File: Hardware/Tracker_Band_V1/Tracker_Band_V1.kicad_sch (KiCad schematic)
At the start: 79 parts, among them J1 USB_C_USB20, Q1 SSM6L56FE, SW1 EVP-AVAA1A, SW2 EVP-AVAA1A, U1 ESP32-C3-MINI-1-N4, U2 BNO085, U3 RT8010, U4 MCP73832-2-AC, U5 LM66200, U6 IN-PI15TAT5R5G5B, U7 IN-PI15TAT5R5G5B, U8 IN-PI15TAT5R5G5B, U9 IN-PI15TAT5R5G5B, X1 32.768kHz

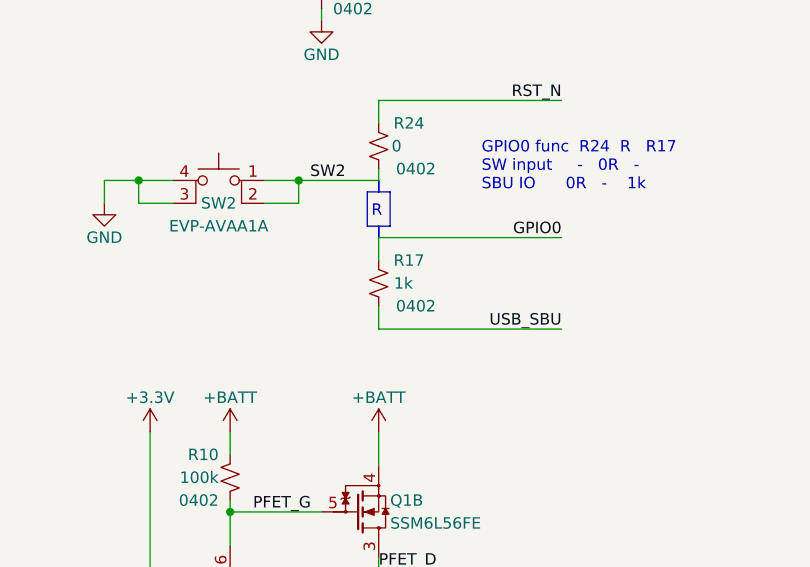
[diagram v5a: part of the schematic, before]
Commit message: Component ordering information finalized
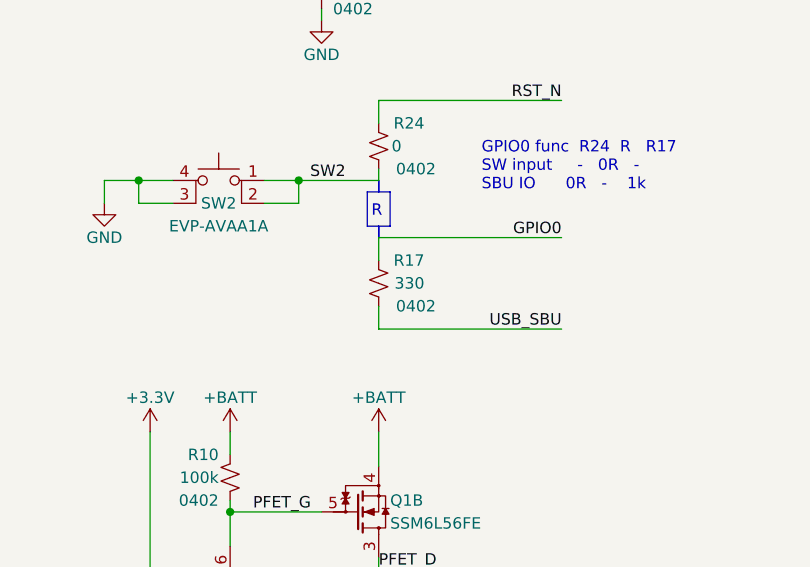
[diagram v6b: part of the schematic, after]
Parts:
- LG1, TP1, TP10, TP11, TP12, TP13, TP14, TP15, TP16, TP17, TP18, TP19, TP2, TP20, TP21, TP3, TP4, TP5, TP6, TP7, TP8, TP9: now left out of the parts list
- R17: value 1k -> 330
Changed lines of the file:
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@@
   )
   (symbol (lib_id "Connector:TestPoint") (at 355.6 81.28 270) (unit 1)
-    (in_bom yes) (on_board yes) (dnp no)
+    (in_bom no) (on_board yes) (dnp no)
     (property "Reference" "TP19" (at 365.76 81.28 90)
       (effects (font (size 1.27 1.27)) (justify left))
@@
   )
   (symbol (lib_id "Connector:TestPoint") (at 355.6 68.58 270) (unit 1)
-    (in_bom yes) (on_board yes) (dnp no)
+    (in_bom no) (on_board yes) (dnp no)
     (property "Reference" "TP14" (at 365.76 68.58 90)
       (effects (font (size 1.27 1.27)) (justify left))
@@
   )
   (symbol (lib_id "Connector:TestPoint") (at 355.6 66.04 270) (unit 1)
-    (in_bom yes) (on_board yes) (dnp no)
+    (in_bom no) (on_board yes) (dnp no)
     (property "Reference" "TP13" (at 365.76 66.04 90)
       (effects (font (size 1.27 1.27)) (justify left))
@@
   )
   (symbol (lib_id "Connector:TestPoint") (at 147.32 260.35 270) (unit 1)
-    (in_bom yes) (on_board yes) (dnp no)
+    (in_bom no) (on_board yes) (dnp no)
     (property "Reference" "TP4" (at 160.02 260.35 90)
       (effects (font (size 1.27 1.27)) (justify left))
@@
   )
   (symbol (lib_id "Connector:TestPoint") (at 355.6 55.88 270) (unit 1)
-    (in_bom yes) (on_board yes) (dnp no)
+    (in_bom no) (on_board yes) (dnp no)
     (property "Reference" "TP9" (at 365.76 55.88 90)
       (effects (font (size 1.27 1.27)) (justify left))
@@
   )
   (symbol (lib_id "Connector:TestPoint") (at 147.32 255.27 270) (unit 1)
-    (in_bom yes) (on_board yes) (dnp no)
+    (in_bom no) (on_board yes) (dnp no)
     (property "Reference" "TP2" (at 160.02 255.27 90)
       (effects (font (size 1.27 1.27)) (justify left))
@@
   )
   (symbol (lib_id "Connector:TestPoint") (at 355.6 53.34 270) (unit 1)
-    (in_bom yes) (on_board yes) (dnp no)
+    (in_bom no) (on_board yes) (dnp no)
     (property "Reference" "TP8" (at 365.76 53.34 90)
       (effects (font (size 1.27 1.27)) (justify left))
@@
   )
   (symbol (lib_id "Connector:TestPoint") (at 355.6 105.41 270) (unit 1)
-    (in_bom yes) (on_board yes) (dnp no)
+    (in_bom no) (on_board yes) (dnp no)
     (property "Reference" "TP5" (at 368.3 105.41 90)
       (effects (font (size 1.27 1.27)) (justify left))
@@
   )
   (symbol (lib_id "Connector:TestPoint") (at 355.6 78.74 270) (unit 1)
-    (in_bom yes) (on_board yes) (dnp no)
+    (in_bom no) (on_board yes) (dnp no)
     (property "Reference" "TP18" (at 365.76 78.74 90)
       (effects (font (size 1.27 1.27)) (justify left))
@@
   )
   (symbol (lib_id "Connector:TestPoint") (at 355.6 107.95 270) (unit 1)
-    (in_bom yes) (on_board yes) (dnp no)
+    (in_bom no) (on_board yes) (dnp no)
     (property "Reference" "TP6" (at 368.3 107.95 90)
       (effects (font (size 1.27 1.27)) (justify left))
@@
   )
   (symbol (lib_id "Connector:TestPoint") (at 355.6 86.36 270) (unit 1)
-    (in_bom yes) (on_board yes) (dnp no)
+    (in_bom no) (on_board yes) (dnp no)
     (property "Reference" "TP21" (at 365.76 86.36 90)
       (effects (font (size 1.27 1.27)) (justify left))
@@
   )
   (symbol (lib_id "Connector:TestPoint") (at 355.6 76.2 270) (unit 1)
-    (in_bom yes) (on_board yes) (dnp no)
+    (in_bom no) (on_board yes) (dnp no)
     (property "Reference" "TP17" (at 365.76 76.2 90)
       (effects (font (size 1.27 1.27)) (justify left))
@@
   )
   (symbol (lib_id "Connector:TestPoint") (at 355.6 71.12 270) (unit 1)
-    (in_bom yes) (on_board yes) (dnp no)
+    (in_bom no) (on_board yes) (dnp no)
     (property "Reference" "TP15" (at 365.76 71.12 90)
       (effects (font (size 1.27 1.27)) (justify left))
@@
   )
   (symbol (lib_id "Connector:TestPoint") (at 355.6 60.96 270) (unit 1)
-    (in_bom yes) (on_board yes) (dnp no)
+    (in_bom no) (on_board yes) (dnp no)
     (property "Reference" "TP11" (at 365.76 60.96 90)
       (effects (font (size 1.27 1.27)) (justify left))
@@
   )
   (symbol (lib_id "Connector:TestPoint") (at 147.32 252.73 270) (unit 1)
-    (in_bom yes) (on_board yes) (dnp no)
+    (in_bom no) (on_board yes) (dnp no)
     (property "Reference" "TP1" (at 160.02 252.73 90)
       (effects (font (size 1.27 1.27)) (justify left))
@@
   )
   (symbol (lib_id "Connector:TestPoint") (at 355.6 58.42 270) (unit 1)
-    (in_bom yes) (on_board yes) (dnp no)
+    (in_bom no) (on_board yes) (dnp no)
     (property "Reference" "TP10" (at 365.76 58.42 90)
       (effects (font (size 1.27 1.27)) (justify left))
@@
   )
   (symbol (lib_id "Connector:TestPoint") (at 355.6 73.66 270) (unit 1)
-    (in_bom yes) (on_board yes) (dnp no)
+    (in_bom no) (on_board yes) (dnp no)
     (property "Reference" "TP16" (at 365.76 73.66 90)
       (effects (font (size 1.27 1.27)) (justify left))
@@
   )
   (symbol (lib_id "Connector:TestPoint") (at 355.6 50.8 270) (unit 1)
-    (in_bom yes) (on_board yes) (dnp no)
+    (in_bom no) (on_board yes) (dnp no)
     (property "Reference" "TP7" (at 365.76 50.8 90)
       (effects (font (size 1.27 1.27)) (justify left))
@@
   )
   (symbol (lib_id "Connector:TestPoint") (at 147.32 257.81 270) (unit 1)
-    (in_bom yes) (on_board yes) (dnp no)
+    (in_bom no) (on_board yes) (dnp no)
     (property "Reference" "TP3" (at 160.02 257.81 90)
       (effects (font (size 1.27 1.27)) (justify left))
@@
   )
   (symbol (lib_id "00_tracker_sym:AB_LOGO") (at 394.97 256.54 0) (unit 1)
-    (in_bom yes) (on_board yes) (dnp no)
+    (in_bom no) (on_board yes) (dnp no)
     (property "Reference" "LG1" (at 392.43 256.54 0)
       (effects (font (size 1.27 1.27)) (justify left))
@@
   )
   (symbol (lib_id "Connector:TestPoint") (at 355.6 83.82 270) (unit 1)
-    (in_bom yes) (on_board yes) (dnp no)
+    (in_bom no) (on_board yes) (dnp no)
     (property "Reference" "TP20" (at 365.76 83.82 90)
       (effects (font (size 1.27 1.27)) (justify left))
@@
       (effects (font (size 1.27 1.27)) (justify left))
     )
-    (property "Value" "1k" (at 229.87 215.9 0)
+    (property "Value" "330" (at 231.14 215.9 0)
       (effects (font (size 1.27 1.27)) (justify left))
     )
@@
   )
   (symbol (lib_id "Connector:TestPoint") (at 355.6 63.5 270) (unit 1)
-    (in_bom yes) (on_board yes) (dnp no)
+    (in_bom no) (on_board yes) (dnp no)
     (property "Reference" "TP12" (at 365.76 63.5 90)
       (effects (font (size 1.27 1.27)) (justify left))
